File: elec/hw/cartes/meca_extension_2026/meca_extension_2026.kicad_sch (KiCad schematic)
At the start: 80 parts, among them J1 2-1445055-3, J14 22272031, J15 22272031, J26 22053051, J27 22053041, Q19 BSS84, Q20 2N7002, U1 TCA9548APWR, U11 LV14340DDAR, U2 PCA9535PW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

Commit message: meca ext : first draft of compenent placement
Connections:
- new net: R19.2, TP1.1, U1.17 (SD6)
- new net: R21.2, TP3.1, U1.19 (SD7)
- new net: R20.2, TP2.1, U1.18 (SC6)
- new net: R22.2, TP4.1, U1.20 (SC7)
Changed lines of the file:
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@@
 	)
 	(junction
-		(at 152.4 93.98)
-		(diameter 0)
-		(color 0 0 0 0)
-	)
-	(junction
 		(at 102.87 213.36)
 		(diameter 0)
@@
 	)
 	(junction
-		(at 160.02 99.06)
-		(diameter 0)
-		(color 0 0 0 0)
-	)
-	(junction
 		(at 114.3 355.6)
 		(diameter 0)
@@
 	)
 	(junction
-		(at 144.78 91.44)
-		(diameter 0)
-		(color 0 0 0 0)
-	)
-	(junction
 		(at 90.17 48.26)
 		(diameter 0)
@@
 	(wire
 		(pts
-			(xy 152.4 40.64) (xy 152.4 93.98)
+			(xy 152.4 40.64) (xy 152.4 99.06)
 		)
 		(stroke
@@
 	(wire
 		(pts
-			(xy 160.02 33.02) (xy 160.02 99.06)
+			(xy 160.02 33.02) (xy 160.02 101.6)
 		)
 		(stroke
@@
 	(wire
 		(pts
-			(xy 160.02 99.06) (xy 160.02 101.6)
-		)
-		(stroke
-			(width 0)
-			(type default)
-		)
-	)
-	(wire
-		(pts
 			(xy 254 129.54) (xy 280.67 129.54)
 		)
@@
 	(wire
 		(pts
-			(xy 144.78 93.98) (xy 152.4 93.98)
-		)
-		(stroke
-			(width 0)
-			(type default)
-		)
-	)
-	(wire
-		(pts
 			(xy 261.62 330.2) (xy 261.62 332.74)
 		)
@@
 	(wire
 		(pts
-			(xy 144.78 91.44) (xy 162.56 91.44)
+			(xy 137.16 91.44) (xy 162.56 91.44)
 		)
 		(stroke
@@
 	(wire
 		(pts
-			(xy 137.16 91.44) (xy 144.78 91.44)
-		)
-		(stroke
-			(width 0)
-			(type default)
-		)
-	)
-	(wire
-		(pts
 			(xy 43.18 31.75) (xy 43.18 33.02)
 		)
@@
 	(wire
 		(pts
-			(xy 152.4 99.06) (xy 160.02 99.06)
-		)
-		(stroke
-			(width 0)
-			(type default)
-		)
-	)
-	(wire
-		(pts
 			(xy 91.44 213.36) (xy 102.87 213.36)
 		)
@@
 	(wire
 		(pts
-			(xy 152.4 93.98) (xy 152.4 99.06)
-		)
-		(stroke
-			(width 0)
-			(type default)
-		)
-	)
-	(wire
-		(pts
 			(xy 254 137.16) (xy 280.67 137.16)
 		)
@@
 	(wire
 		(pts
-			(xy 152.4 93.98) (xy 162.56 93.98)
+			(xy 144.78 93.98) (xy 162.56 93.98)
 		)
 		(stroke
@@
 	(wire
 		(pts
-			(xy 160.02 99.06) (xy 162.56 99.06)
+			(xy 152.4 99.06) (xy 162.56 99.06)
 		)
 		(stroke
@@
 	(wire
 		(pts
-			(xy 144.78 91.44) (xy 144.78 93.98)
+			(xy 144.78 33.02) (xy 144.78 93.98)
 		)
 		(stroke
@@
 		)
 		(stroke
-			(width 0)
-			(type default)
-		)
-	)
-	(wire
-		(pts
-			(xy 144.78 33.02) (xy 144.78 91.44)
-		)
-		(stroke

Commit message: meca_extension : connectors placement modified
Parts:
- added C32: 1µF 50V, cocotter_capacitors:C_0805_2012Metric, symbol cocotter_capacitors:C_1µF_50V_0805
- added H1, H2, H3, H4, H5: MountingHole_Pad_M3, cocotter_others:MountingHole_3.2mm_M3_Pad_Via, symbol cocotter_others:MountingHole_Pad_M3
- added J16: 5264-3P, cocotter_connectors:5264-3P, symbol cocotter_connectors:feetech_servo
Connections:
- net +6V: now also C32.1, J16.2 (VCC)
- net GND: now also C32.2, H1.1, H2.1, H3.1, H4.1, H5.1, J16.1 (GND)
- net digital_servo_cmd_3v3: now also J16.3 (SIG)
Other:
- note added: "Top level servo connector"

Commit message: meca_extension: implant modified and integrated into CAD
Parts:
- J26: footprint cocotter_connectors:22053051 -> cocotter_connectors:22272051; symbol cocotter_connectors:22053051 -> cocotter_connectors:22272051; JLCPCB Part # C586992 -> C585785
- J27: footprint cocotter_connectors:22053041 -> cocotter_connectors:22272041; symbol cocotter_connectors:22053041 -> cocotter_connectors:22272041; JLCPCB Part # C5271241 -> C504991
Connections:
- net +3.3V: now also J27.3; no longer J27.4
- net GND: no longer J27.1
- net scl_3v3: now also J27.1; no longer J27.2
- net sda_3v3: now also J27.2; no longer J27.3
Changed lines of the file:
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@@
 	)
 	(symbol
-		(lib_id "cocotter_connectors:22053041")
+		(lib_id "cocotter_connectors:22272041")
 		(at 25.4 72.39 0)
 		(unit 1)
@@
 		(fields_autoplaced yes)
 		(property "Reference" "J27"
-			(at 19.685 63.5 0)
+			(at 21.59 59.69 0)
 			(effects
 				(font
@@
 		)
 		(property "Value" "22053041"
-			(at 19.685 66.04 0)
+			(at 21.59 62.23 0)
 			(effects
 				(font
@@
 			)
 		)
-		(property "Footprint" "cocotter_connectors:22053041"
-			(at 25.4 72.39 0)
+		(property "Footprint" "cocotter_connectors:22272041"
+			(at 22.098 84.328 0)
 			(effects
 				(font
@@
 			)
 		)
-		(property "Datasheet" ""
-			(at 25.4 72.39 0)
+		(property "Datasheet" "https://www.molex.com/en-us/products/part-detail/22272041"
+			(at 25.4 81.28 0)
 			(effects
 				(font
@@
 			)
 		)
-		(property "Description" "mini KK, 2.54mm pitch, 4 ways, right angle"
-			(at 25.4 72.39 0)
+		(property "Description" "mini kk 4 voies vertical"
+			(at 25.4 81.28 0)
 			(effects
 				(font
@@
 			)
 		)
-		(property "JLCPCB Part #" "C5271241"
+		(property "JLCPCB Part #" "C504991"
 			(at 25.4 72.39 0)
 			(effects
@@
 	)
 	(symbol
-		(lib_id "cocotter_connectors:22053051")
+		(lib_id "cocotter_connectors:22272051")
 		(at 25.4 128.27 0)
 		(unit 1)
@@
 		(fields_autoplaced yes)
 		(property "Reference" "J26"
-			(at 19.685 116.84 0)
+			(at 21.59 115.57 0)
 			(effects
 				(font
@@
 		)
 		(property "Value" "22053051"
-			(at 19.685 119.38 0)
+			(at 21.59 118.11 0)
 			(effects
 				(font
@@
 			)
 		)
-		(property "Footprint" "cocotter_connectors:22053051"
-			(at 25.4 128.27 0)
+		(property "Footprint" "cocotter_connectors:22272051"
+			(at 22.098 140.208 0)
 			(effects
 				(font
@@
 			)
 		)
-		(property "Datasheet" ""
-			(at 25.4 128.27 0)
+		(property "Datasheet" "https://www.molex.com/en-us/products/part-detail/22272051"
+			(at 25.4 137.16 0)
 			(effects
 				(font
@@
 			)
 		)
-		(property "Description" "mini KK, 2.54mm pitch, 5ways, right angle"
-			(at 25.4 128.27 0)
+		(property "Description" "mini kk 5 voies vertical"
+			(at 25.4 137.16 0)
 			(effects
 				(font
@@
 			)
 		)
-		(property "JLCPCB Part #" "C586992"
+		(property "JLCPCB Part #" "C585785"
 			(at 25.4 128.27 0)
 			(effects

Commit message: meca_extension : battery connector changed
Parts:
- J1: value 2-1445055-3 -> 2-1445051-3; footprint cocotter_connectors:2-1445055-3 -> cocotter_connectors:2-1445051-3; symbol cocotter_connectors:2-1445055-3 -> cocotter_connectors:2-1445051-3; JLCPCB Part # C239447 -> C17473329
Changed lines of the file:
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@@
 	)
 	(symbol
-		(lib_id "cocotter_connectors:2-1445055-3")
-		(at 21.59 36.83 0)
+		(lib_id "cocotter_connectors:2-1445051-3")
+		(at 21.59 35.56 0)
 		(mirror x)
 		(unit 1)
@@
 		(dnp no)
 		(property "Reference" "J1"
-			(at 20.9551 30.48 90)
+			(at 19.304 40.386 0)
 			(effects
 				(font
 					(size 1.27 1.27)
 				)
-				(justify right)
 			)
 		)
-		(property "Value" "2-1445055-3"
-			(at 18.4151 30.48 90)
+		(property "Value" "2-1445051-3"
+			(at 16.256 32.258 90)
 			(effects
 				(font
 					(size 1.27 1.27)
 				)
-				(justify right)
 			)
 		)
-		(property "Footprint" "cocotter_connectors:2-1445055-3"
-			(at 17.78 39.37 0)
+		(property "Footprint" "cocotter_connectors:2-1445051-3"
+			(at 17.78 38.1 0)
 			(effects
 				(font
@@
 			)
 		)
-		(property "Description" "1x3POS micro Mate'n LOK, through hole, right angle"
-			(at 17.78 39.37 0)
+		(property "Description" "1x3POS micro Mate'n LOK, through hole, vertical"
+			(at 17.78 38.1 0)
 			(effects
 				(font
@@
 			)
 		)
-		(property "JLCPCB Part #" "C239447"
-			(at 21.59 36.83 0)
+		(property "JLCPCB Part #" "C17473329"
+			(at 21.59 35.56 0)
 			(effects
 				(font

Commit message: meca_extension : led added and J1 moved
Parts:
- added D9: yellow, 0603, cocotter_diodes:LED_0603_1608Metric, symbol cocotter_diodes:yellow_led_0603
- added R57: 1k 1%, cocotter_resistor:r0603_reflow, symbol cocotter_resistors:R_1k_0603_1%
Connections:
- net GND: now also D9.C
- net at U2.11 (IO0_7): now also R57.1
- new net: D9.A, R57.2

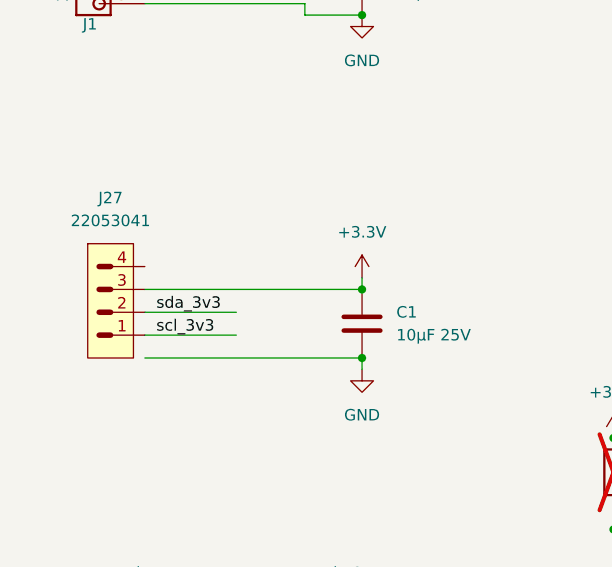
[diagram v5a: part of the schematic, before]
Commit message: meca_extension : led added and J1 moved
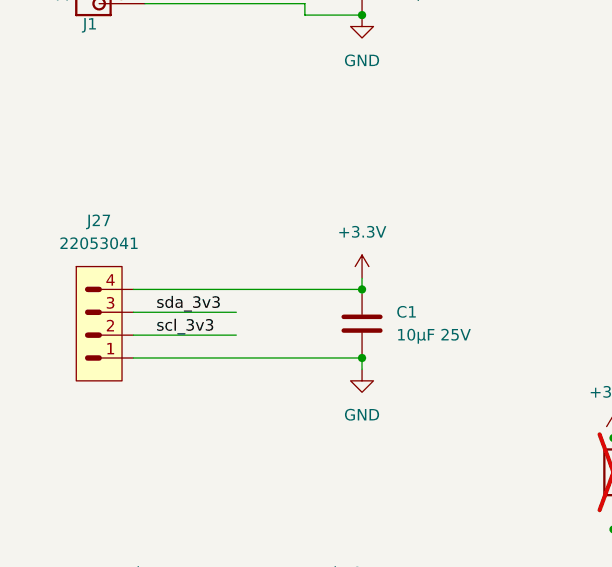
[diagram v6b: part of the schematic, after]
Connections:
- net +3.3V: now also J27.4; no longer J27.3
- net GND: now also J27.1
- net scl_3v3: now also J27.2; no longer J27.1
- net sda_3v3: now also J27.3; no longer J27.2
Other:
- moved on the sheet: J27
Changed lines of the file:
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@@
 	(wire
 		(pts
-			(xy 25.4 77.47) (xy 49.53 77.47)
-		)
-		(stroke
-			(width 0)
-			(type default)
-		)
-	)
-	(wire
-		(pts
 			(xy 130.81 60.96) (xy 168.91 60.96)
 		)
@@
 	(wire
 		(pts
-			(xy 25.4 74.93) (xy 35.56 74.93)
+			(xy 24.13 74.93) (xy 35.56 74.93)
 		)
 		(stroke
@@
 	(wire
 		(pts
-			(xy 25.4 72.39) (xy 35.56 72.39)
+			(xy 24.13 72.39) (xy 35.56 72.39)
 		)
 		(stroke
@@
 	(wire
 		(pts
+			(xy 24.13 77.47) (xy 49.53 77.47)
+		)
+		(stroke
+			(width 0)
+			(type default)
+		)
+	)
+	(wire
+		(pts
 			(xy 232.41 355.6) (xy 246.38 355.6)
 		)
@@
 	(wire
 		(pts
-			(xy 25.4 69.85) (xy 49.53 69.85)
+			(xy 24.13 69.85) (xy 49.53 69.85)
 		)
 		(stroke
@@
 	(symbol
 		(lib_id "cocotter_connectors:22272041")
-		(at 25.4 72.39 0)
+		(at 24.13 74.93 0)
 		(unit 1)
 		(exclude_from_sim no)
@@
 		(fields_autoplaced yes)
 		(property "Reference" "J27"
-			(at 21.59 59.69 0)
+			(at 20.32 62.23 0)
 			(effects
 				(font
@@
 		)
 		(property "Value" "22053041"
-			(at 21.59 62.23 0)
+			(at 20.32 64.77 0)
 			(effects
 				(font
@@
 		)
 		(property "Footprint" "cocotter_connectors:22272041"
-			(at 22.098 84.328 0)
+			(at 20.828 86.868 0)
 			(effects
 				(font
@@
 		)
 		(property "Datasheet" "https://www.molex.com/en-us/products/part-detail/22272041"
-			(at 25.4 81.28 0)
+			(at 24.13 83.82 0)
 			(effects
 				(font
@@
 		)
 		(property "Description" "mini kk 4 voies vertical"
-			(at 25.4 81.28 0)
+			(at 24.13 83.82 0)
 			(effects
 				(font
@@
 		)
 		(property "JLCPCB Part #" "C504991"
-			(at 25.4 72.39 0)
+			(at 24.13 74.93 0)
 			(effects
 				(font
@@
 		)
 		(instances
-			(project ""
+			(project "meca_extension_2026"
 				(path "/f6dc6b20-ab52-4b2b-893a-1fb4f3ec4277"
 					(reference "J27")

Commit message: meca_ext: layout almost done
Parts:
- added R58, R59, R60, R61: 2k2 1%, cocotter_resistor:r0603_reflow, symbol cocotter_resistors:R_2k2_0603_1%
- added TP5, TP6, TP7, TP8: TestPoint, cocotter_others:testpoint-THT-0.8mm, symbol cocotter_others:TestPoint_0.8mm
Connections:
- net +3.3V: now also R58.1, R59.1, R60.1, R61.1
- net scl_4_3v3: no longer names the net of U1.14 (SC4)
- net scl_4_3v3: now also R61.2, TP8.1
- net scl_5_3v3: no longer names the net of U1.16 (SC5)
- net scl_5_3v3: now also R59.2, TP6.1
- net sda_4_3v3: no longer names the net of U1.13 (SD4)
- net sda_4_3v3: now also R60.2, TP7.1
- net sda_5_3v3: no longer names the net of U1.15 (SD5)
- net sda_5_3v3: now also R58.2, TP5.1
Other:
- moved on the sheet: TP1, TP2, TP3, TP4

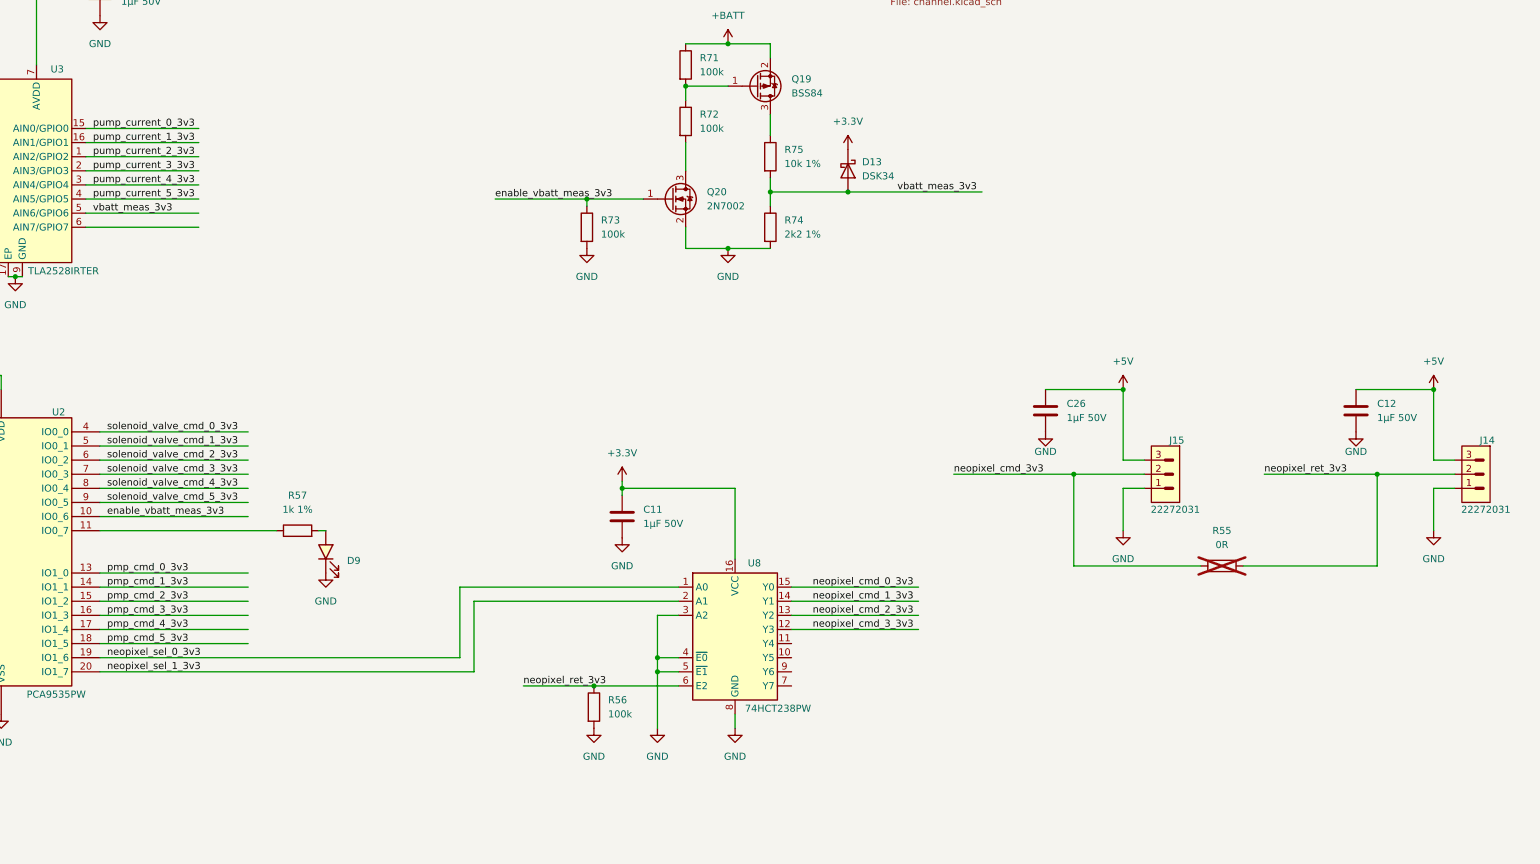
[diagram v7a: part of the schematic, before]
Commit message: meca_extension routing review and schematic correction
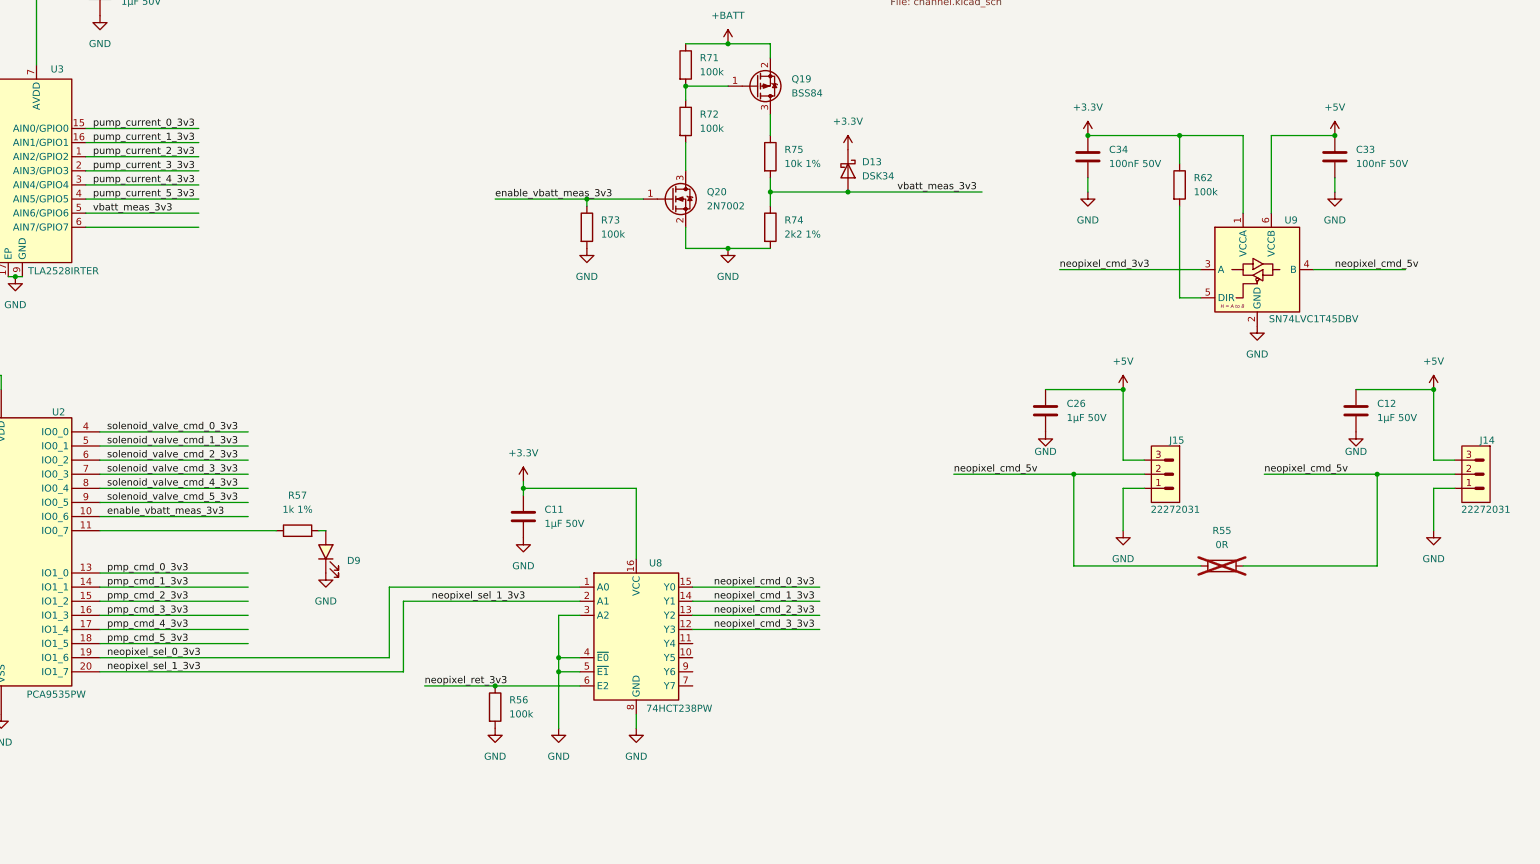
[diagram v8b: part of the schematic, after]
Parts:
- added C33, C34: 100nF 50V, cocotter_capacitors:C_0603_1608Metric, symbol cocotter_capacitors:C_100nF_50V_0603
- added R62: 100k, cocotter_resistor:r0603_reflow, symbol cocotter_resistors:R_100k_0603_1%
- added U9: SN74LVC1T45DBV, Package_TO_SOT_SMD:SOT-23-6, symbol cocotter_ic:SN74LVC1T45DBV
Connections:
- net +3.3V: now also C34.1, R62.1, U9.1 (VCCA)
- net +5V: now also C33.1, U9.6 (VCCB)
- net GND: now also C33.2, C34.2, U9.2 (GND)
- net neopixel_cmd_3v3: now also U9.3 (A); no longer J15.2, R55.1
- net neopixel_ret_3v3: no longer J14.2, R55.2
- new net: R62.2, U9.5 (DIR)
- new net neopixel_cmd_5v: J14.2, J15.2, R55.1, R55.2, U9.4 (B)
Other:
- moved on the sheet: C11, R56, U8
